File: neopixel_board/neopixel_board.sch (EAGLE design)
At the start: 50 parts, among them J1 SSW-102-02-T-S-RA, J2 SSW-102-02-T-S-RA, J3 SSW-102-02-T-S-RA, J4 SSW-102-02-T-S-RA, J5 1981584-1, U2 MIC5219, Y1 16MHz

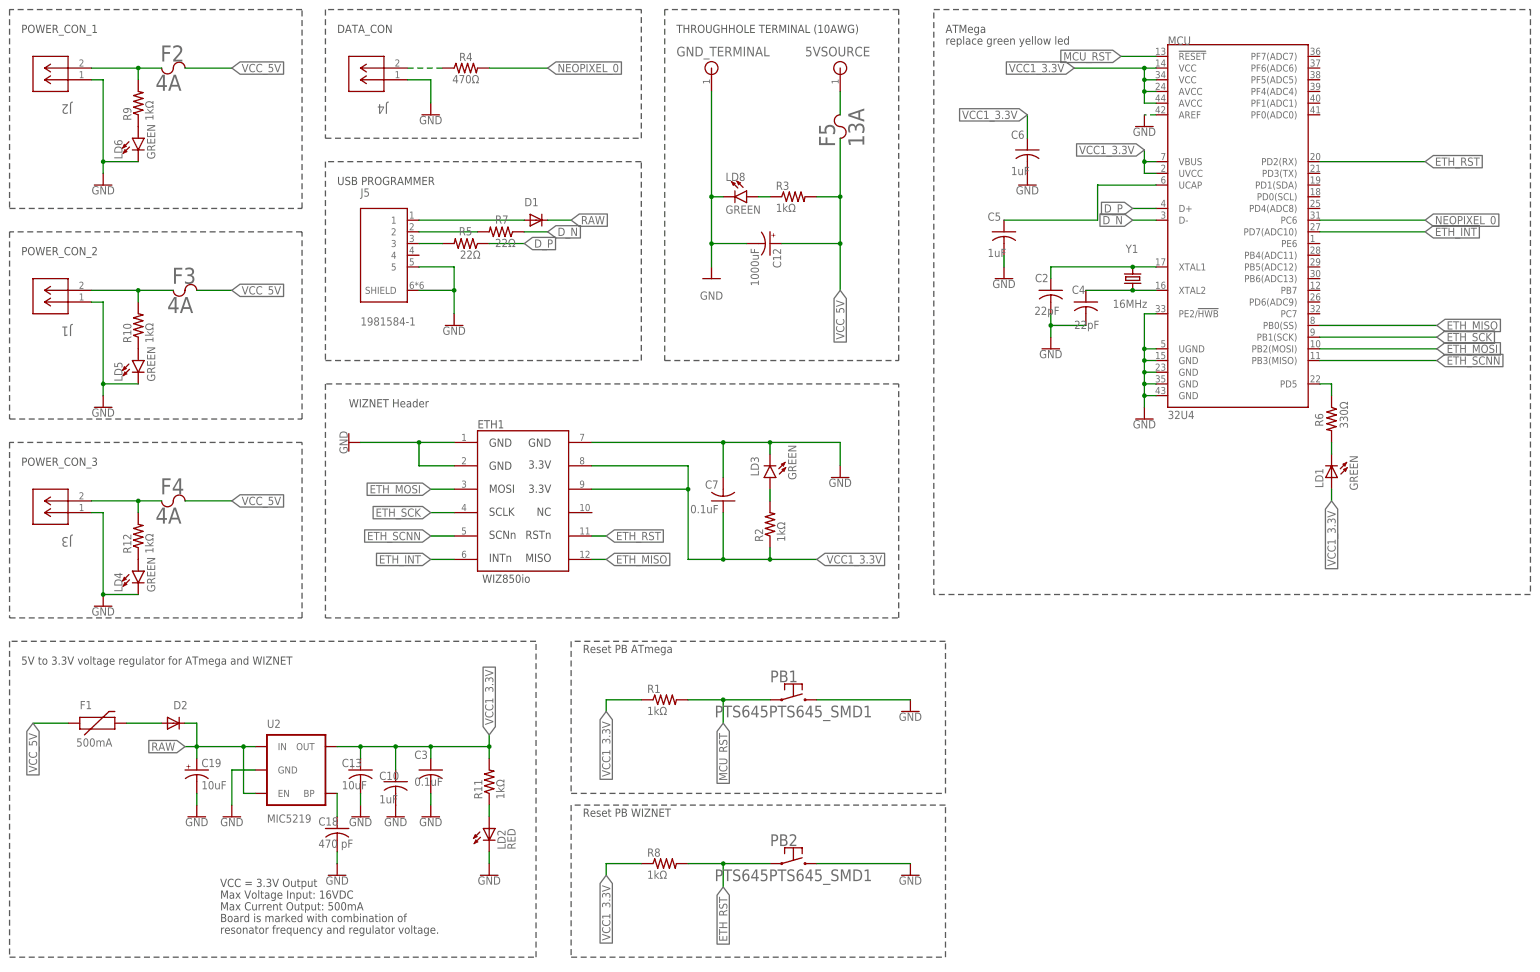
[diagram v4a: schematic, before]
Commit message: Schematic WIP
addressing W.S. critique
NOTE: in changing voltage tags to symbols, BRD routes are lost
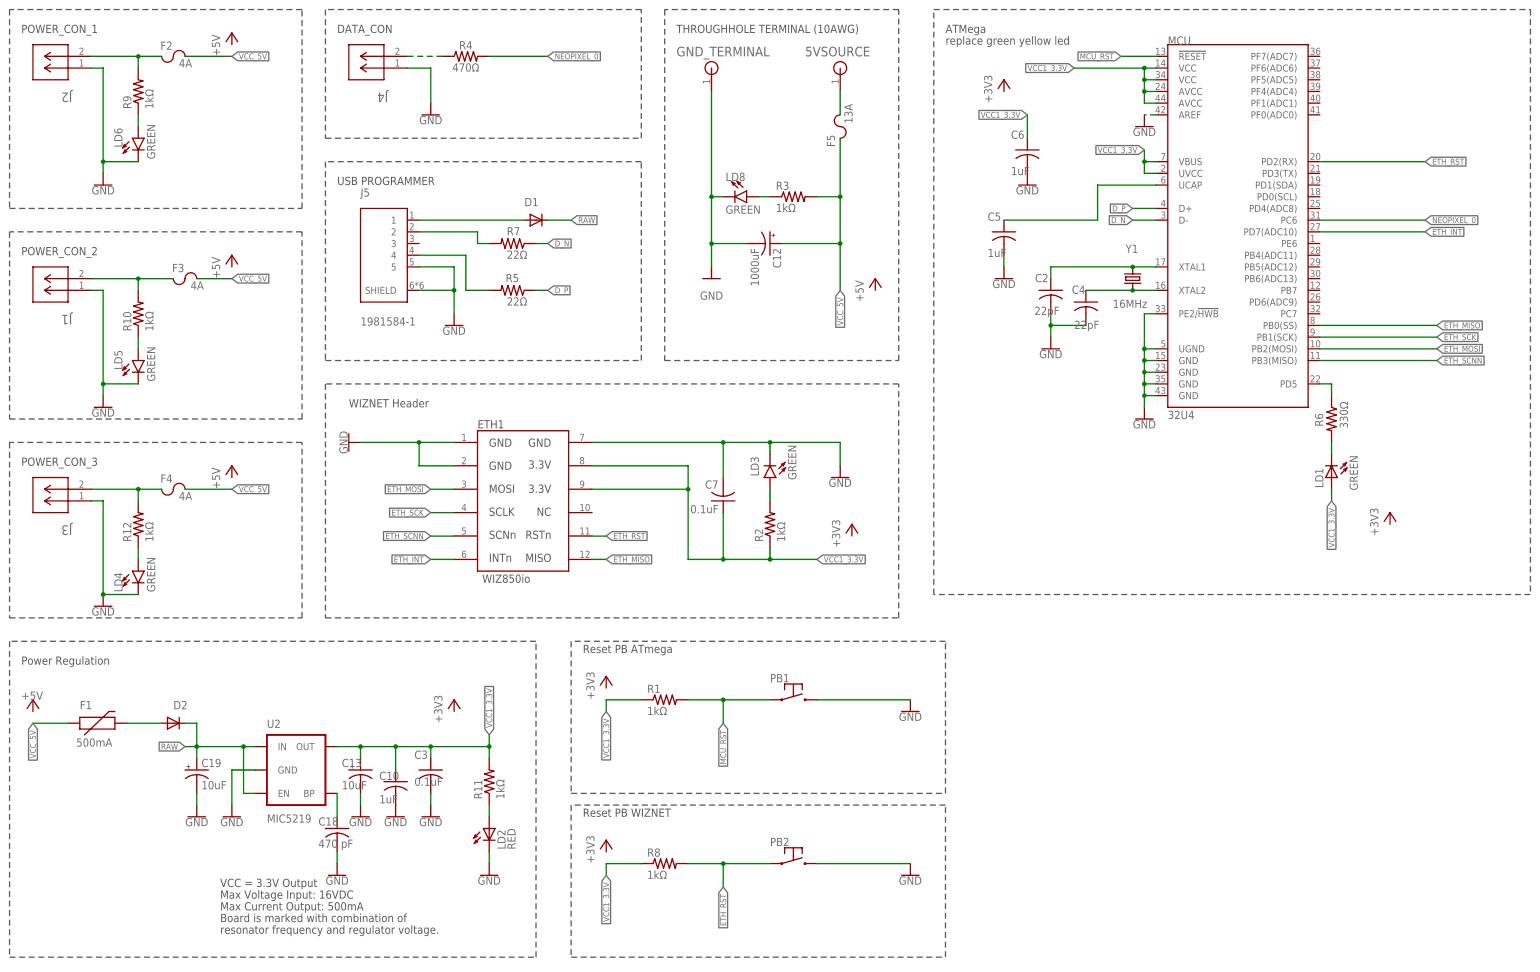
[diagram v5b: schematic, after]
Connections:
- removed net N$8: J5.3, R5.2
- new net N$3: J5.4, R5.2
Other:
- note added: "Power Regulation"
- note removed: "5V to 3.3V voltage regulator for ATmega and WIZNET"
- moved on the sheet: F2, F3, F4, J1, J2, J3, J4, R10, R12, R4, R5, R7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

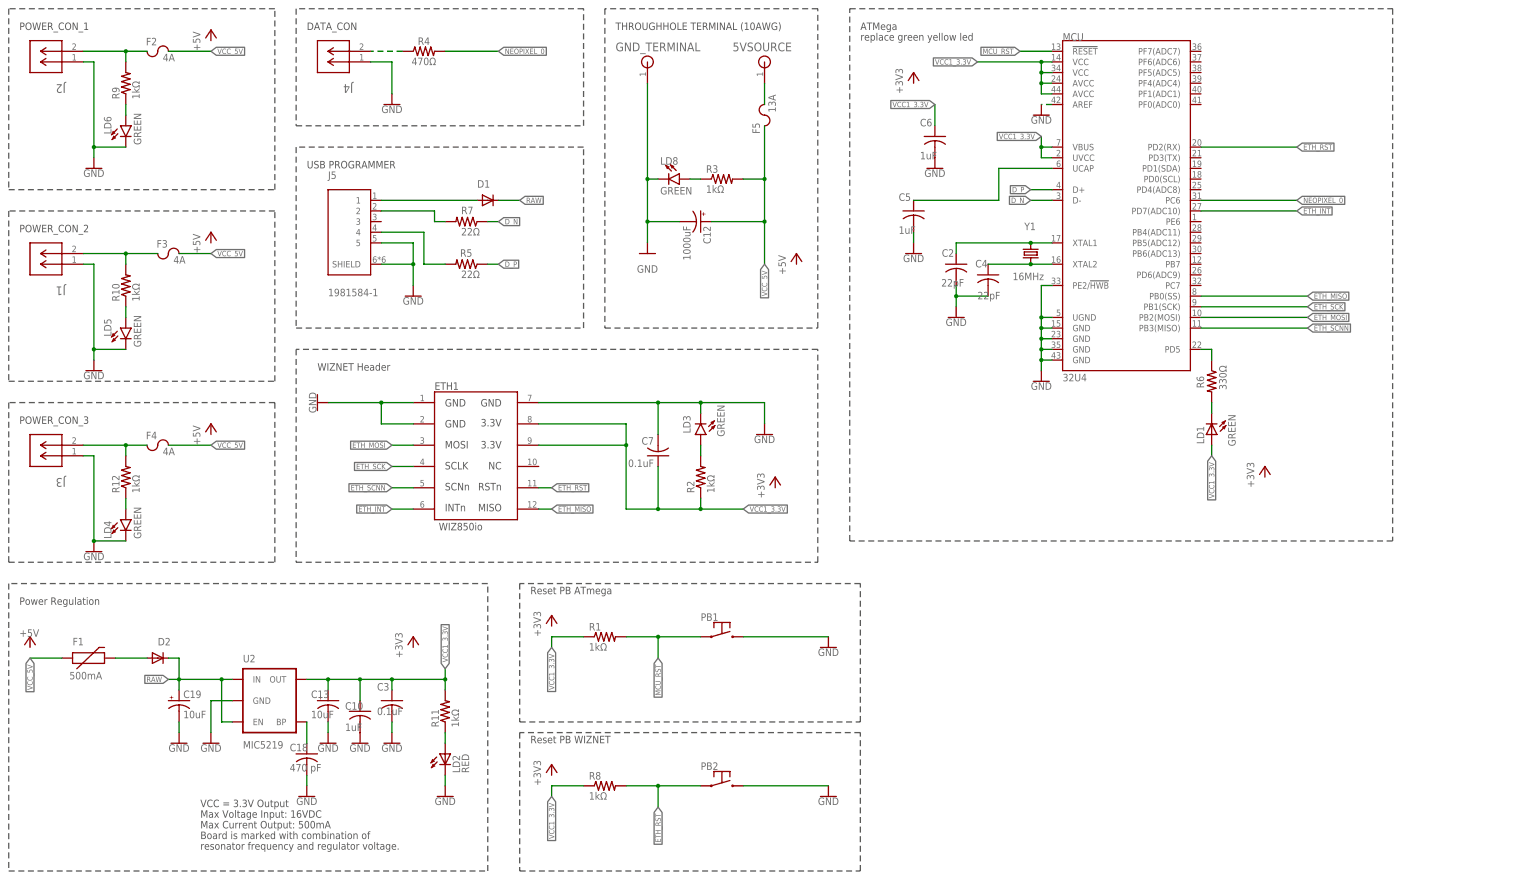
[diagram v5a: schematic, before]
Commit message: Schematic updates
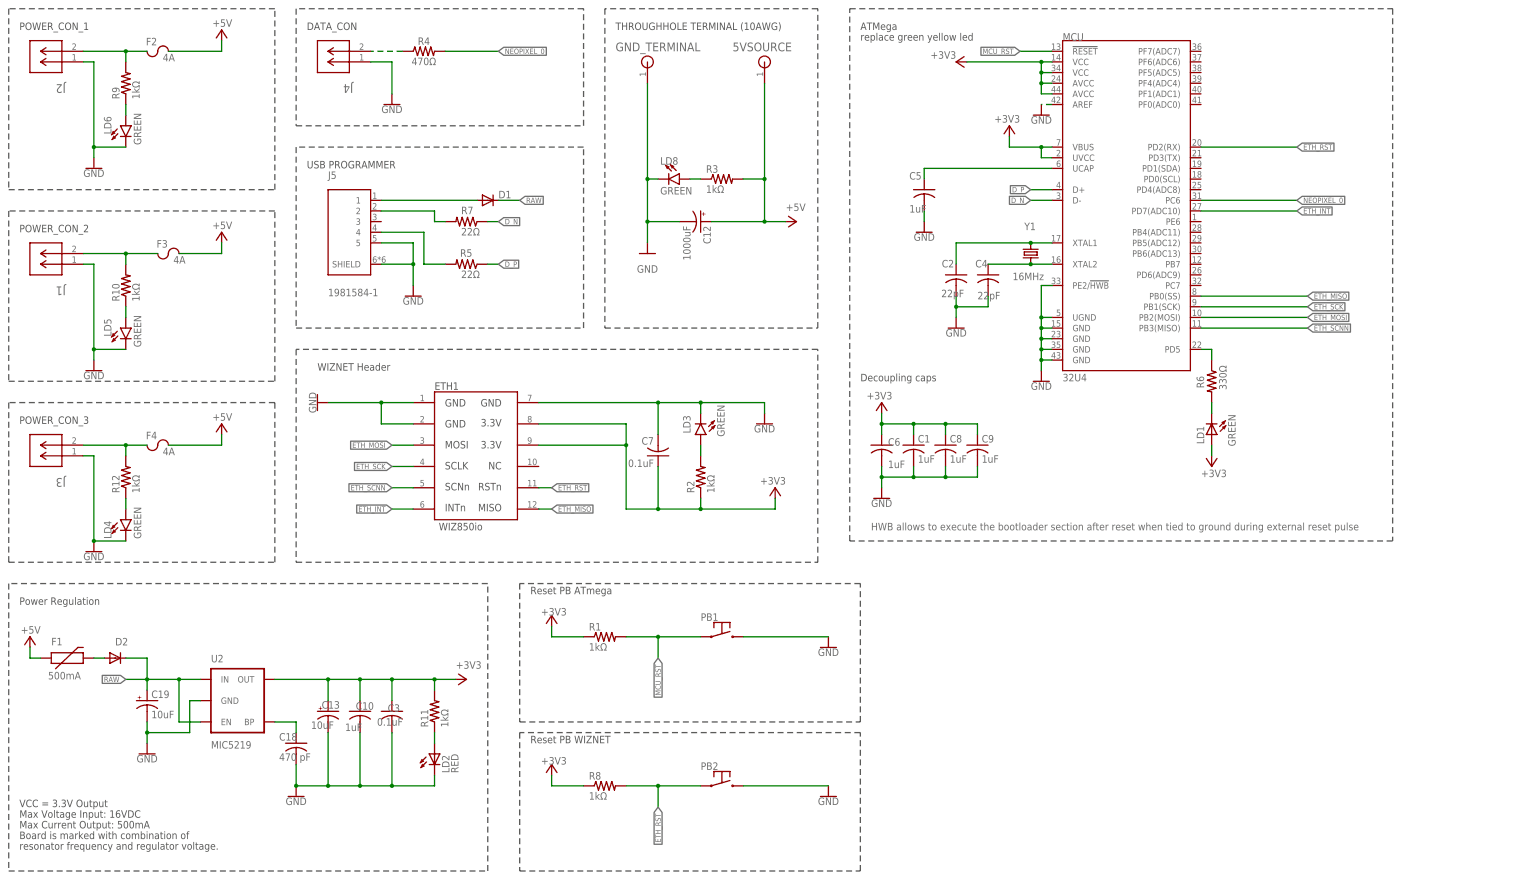
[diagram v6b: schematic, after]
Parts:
- removed F5: 13A, neopixel_board:3557-2
- added C1, C8, C9: 1uF, rcl:C-USC0603
- D1: device diode:DIODE-SOD110-W -> SparkFun:DIODESOD
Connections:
- removed net 5VIN: 5VSOURCE.1, F5.1
- removed net VCC1_3.3V: C10.1, C13.+, C3.1, C6.1, C7.1, ETH1.8, ETH1.9, LD1.A, MCU.AVCC@24, MCU.AVCC@44, MCU.UVCC, MCU.VBUS, MCU.VCC@14, MCU.VCC@34, R1.1, R11.2, R2.1, R8.1, U2.OUT
- removed net VCC_5V: C12.+, F1.1, F2.2, F3.2, F4.2, F5.2, R3.2
- new net +3V3: C1.1, C10.1, C13.+, C3.1, C6.1, C7.1, C8.1, C9.1, ETH1.8, ETH1.9, LD1.A, MCU.AVCC@24, MCU.AVCC@44, MCU.UVCC, MCU.VBUS, MCU.VCC@14, MCU.VCC@34, R1.1, R11.2, R2.1, R8.1, U2.OUT
- new net +5V: 5VSOURCE.1, C12.+, F1.1, F2.2, F3.2, F4.2, R3.2
- net GND: now also C1.2, C8.2, C9.2
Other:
- note added: "Decoupling caps"
- note added: "HWB allows to execute the bootloader section after reset when tied to ground during external reset pulse"
- moved on the sheet: C13, C18, C19, C2, C3, C5, C6, D2, F1, LD2, R11, U2

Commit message: BRD and SCH ready for review
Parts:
- renumbered C18 to C14, C19 to C11, LD8 to LD7

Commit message: Pre-design review corrections
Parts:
- LD1: value GREEN -> BLUE
- LD2: value RED -> GREEN
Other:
- note removed: "replace green yellow led"
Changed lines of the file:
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@@
 <part name="C13" library="SparkFun" deviceset="CAP_POL" device="1206" value="10uF"/>
 <part name="R11" library="SparkFun" deviceset="RESISTOR" device="0603-RES" value="1kΩ"/>
-<part name="LD2" library="SparkFun" deviceset="LED" device="0603" value="RED"/>
+<part name="LD2" library="SparkFun" deviceset="LED" device="0603" value="GREEN"/>
 <part name="C3" library="rcl" library_urn="urn:adsk.eagle:library:334" deviceset="C-US" device="C0603" package3d_urn="urn:adsk.eagle:package:23616/2" value="0.1uF"/>
 <part name="R6" library="SparkFun" deviceset="RESISTOR" device="0603-RES" value="330Ω"/>
-<part name="LD1" library="SparkFun" deviceset="LED" device="0603" value="GREEN"/>
+<part name="LD1" library="SparkFun" deviceset="LED" device="0603" value="BLUE"/>
 <part name="U2" library="SparkFun" deviceset="V_REG_LDO" device="SMD" value="MIC5219"/>
 <part name="C11" library="SparkFun" deviceset="CAP_POL" device="1206" value="10uF"/>
@@
 <text x="248.92" y="236.22" size="1.778" layer="97">ATMega</text>
 <text x="190.5" y="236.22" size="1.778" layer="97">THROUGHHOLE TERMINAL (10AWG)</text>
-<text x="248.92" y="233.68" size="1.778" layer="97">replace green yellow led</text>
 <wire x1="167.64" y1="68.58" x2="167.64" y2="35.56" width="0.1524" layer="97" style="longdash"/>
 <wire x1="167.64" y1="35.56" x2="248.92" y2="35.56" width="0.1524" layer="97" style="longdash"/>
